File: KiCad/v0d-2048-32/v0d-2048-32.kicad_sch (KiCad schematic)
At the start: 24 parts, among them U1 AM29F160, U10 IS62C256AL, U13 74HC40103, U2 74HC139, U3 74HC273, U4 74HC4520, U5 74HC139, U7 74HC670, U9 IS62C256AL

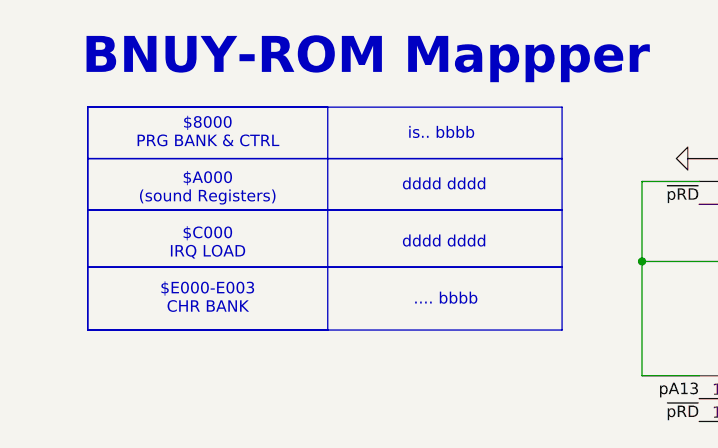
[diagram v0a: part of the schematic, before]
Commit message: schematic tweak
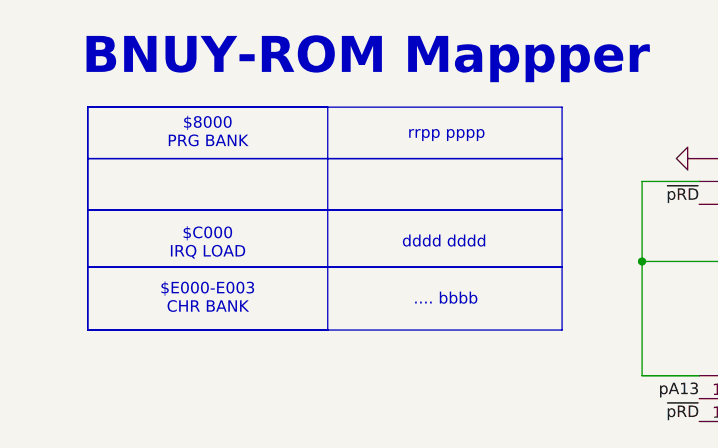
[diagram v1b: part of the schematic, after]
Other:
- note added: "rrpp pppp"
- note removed: "is.. bbbb"
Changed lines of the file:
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@@
 		(title "BNUY-ROM Board")
 		(date "2025-06-30")
-		(rev "v0c")
+		(rev "v0d")
 	)
 	(rectangle
@@
 		)
 	)
-	(text "is.. bbbb"
+	(text "rrpp pppp"
 		(exclude_from_sim no)
 		(at 52.705 27.305 0)
@@
 		)
 	)
-	(text "dddd dddd"
-		(exclude_from_sim no)
-		(at 52.07 33.02 0)
-		(effects
-			(font
-				(size 1.27 1.27)
-			)
-			(justify left bottom)
-		)
-	)
 	(text "CHR LATCH"
 		(exclude_from_sim no)
@@
 		)
 	)
-	(text_box "$8000\nPRG BANK & CTRL\n\n$A000\n(sound Registers)\n\n$C000\nIRQ LOAD\n\n$E000-E003\nCHR BANK"
+	(text_box "$8000\nPRG BANK\n\n\n\n\n$C000\nIRQ LOAD\n\n$E000-E003\nCHR BANK"
 		(exclude_from_sim no)
 		(at 17.145 23.495 0)
